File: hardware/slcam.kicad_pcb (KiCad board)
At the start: 4 copper layers, 42.2 x 25.4 mm, 33 parts, among them J1 532610671, J2 Conn_01x08, J3 Conn_01x04, J4 532610371, J5 532610371, U1 STM32F103C8Tx, U2 W25Q128JVS, U3 TCAN330G, U4 TPS2044D, Y1 Crystal_GND24

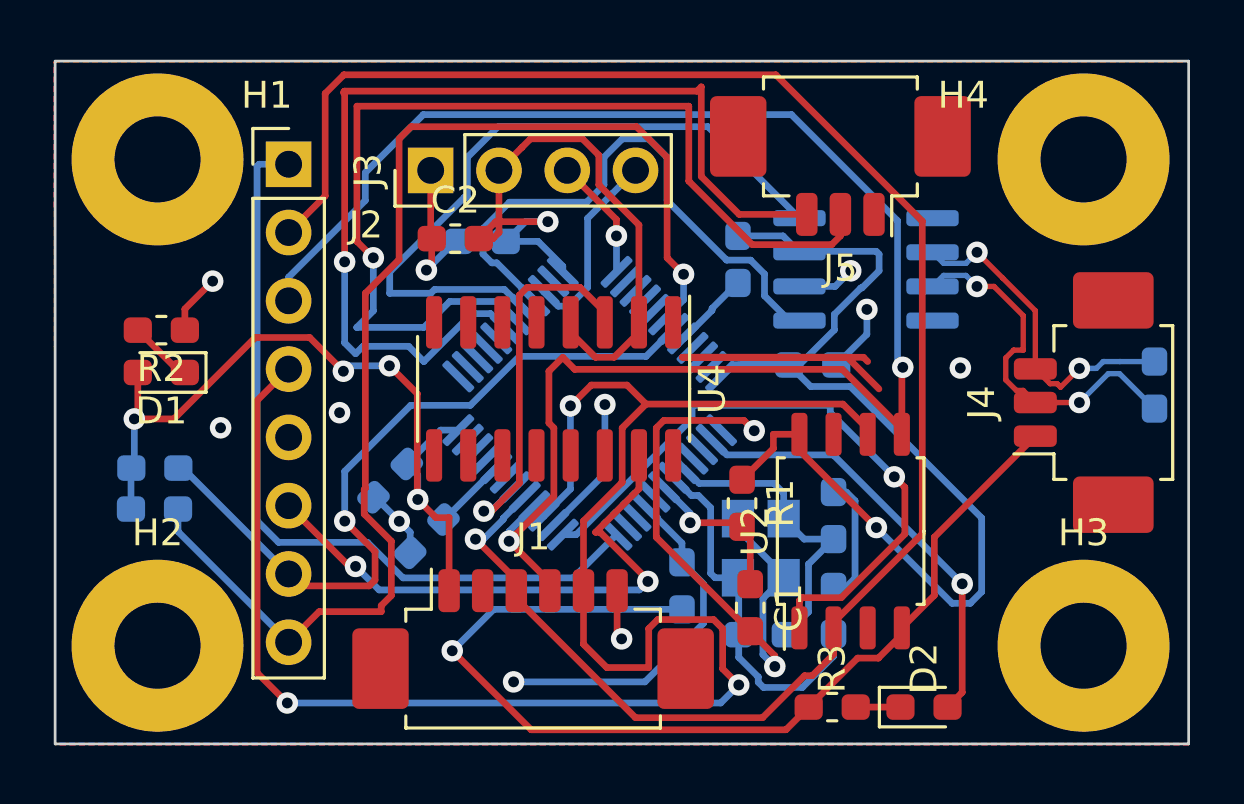
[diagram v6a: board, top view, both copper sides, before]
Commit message: hardware: Fixing the position of some labels in the layout #29
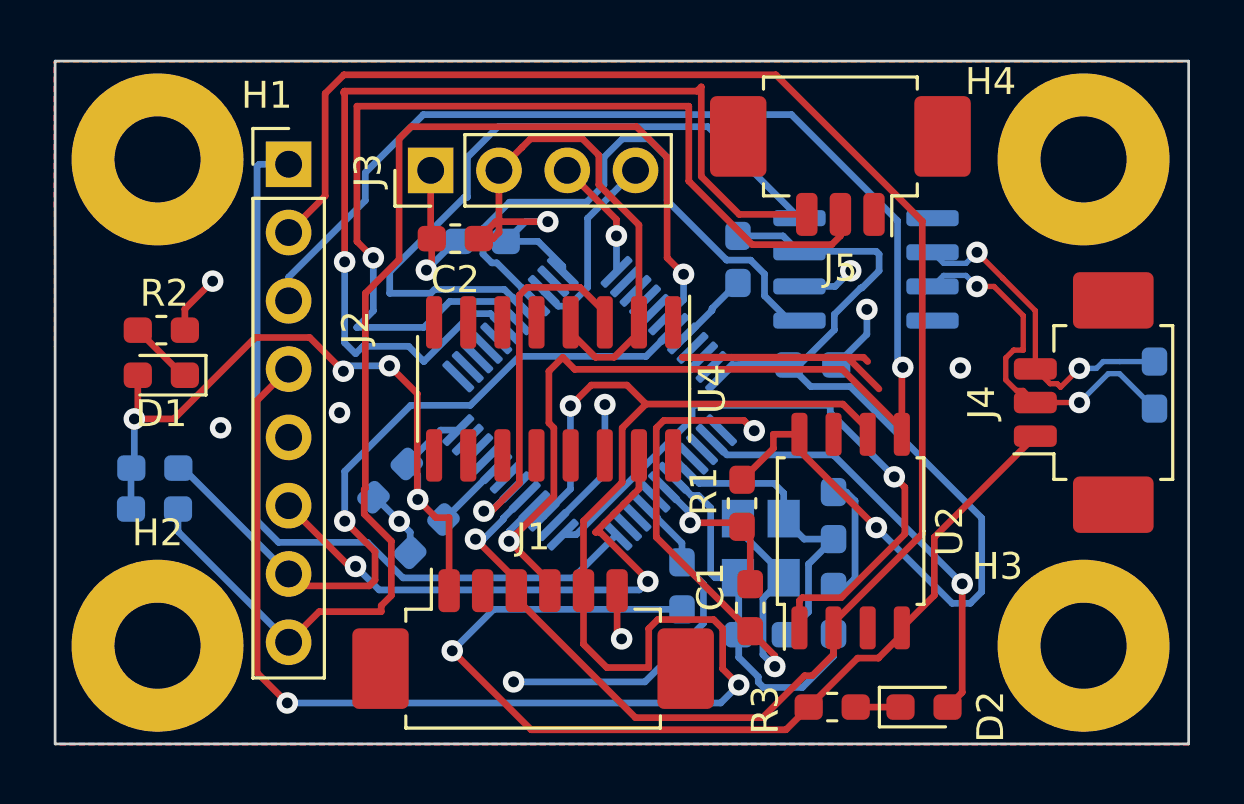
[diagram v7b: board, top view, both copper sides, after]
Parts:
- moved D1 0.10 mm to (201.1, 61.5)
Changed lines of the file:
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@@
     (tags "Through hole pin header THT 1x08 2.54mm single row")
     (attr through_hole)
-    (fp_text reference "J2" (at 2.871 2.26) (layer "F.SilkS")
+    (fp_text reference "J2" (at 2.49 6.07 90) (layer "F.SilkS")
       (effects (font (size 1 1) (thickness 0.15)))
     )
@@
     (tags "SOIC SO")
     (attr smd)
-    (fp_text reference "U2" (at 0 -3.56 270) (layer "F.SilkS")
+    (fp_text reference "U2" (at 0 3.683 270) (layer "F.SilkS")
       (effects (font (size 1 1) (thickness 0.15)))
     )
@@
     (tags "mounting hole 3.2mm m3")
     (attr exclude_from_pos_files exclude_from_bom)
-    (fp_text reference "H3" (at 0 -4.2) (layer "F.SilkS")
+    (fp_text reference "H3" (at -3.204 -2.95) (layer "F.SilkS")
       (effects (font (size 1 1) (thickness 0.15)))
     )
@@
     (tags "mounting hole 3.2mm m3")
     (attr exclude_from_pos_files exclude_from_bom)
-    (fp_text reference "H4" (at -4.474 -2.386) (layer "F.SilkS")
+    (fp_text reference "H4" (at -3.458 -2.894) (layer "F.SilkS")
       (effects (font (size 1 1) (thickness 0.15)))
     )
@@
     (tags "capacitor handsolder")
     (attr smd)
-    (fp_text reference "C1" (at 0 -1.43 90) (layer "F.SilkS")
+    (fp_text reference "C1" (at -0.7734 1.4732 90) (layer "F.SilkS")
       (effects (font (size 1 1) (thickness 0.15)))
     )
@@
   )
   (footprint "LED_SMD:LED_0603_1608Metric_Pad1.05x0.95mm_HandSolder" (layer "F.Cu")
-    (at 201.055 61.3664 180)
+    (at 201.055 61.468 180)
     (descr "LED SMD 0603 (1608 Metric), square (rectangular) end terminal, IPC_7351 nominal, (Body size source: http://www.tortai-tech.com/upload/download/2011102023233369053.pdf), generated with kicad-footprint-generator")
     (tags "LED handsolder")
@@
     (tags "resistor handsolder")
     (attr smd)
-    (fp_text reference "R1" (at 0 -1.43 90) (layer "F.SilkS")
+    (fp_text reference "R1" (at -0.4458 1.4224 90) (layer "F.SilkS")
       (effects (font (size 1 1) (thickness 0.15)))
     )
@@
     (tags "resistor handsolder")
     (attr smd)
-    (fp_text reference "R2" (at 0 -1.43) (layer "F.SilkS")
+    (fp_text reference "R2" (at -0.113 1.3716) (layer "F.SilkS")
       (effects (font (size 1 1) (thickness 0.15)))
     )
@@
     (tags "resistor handsolder")
     (attr smd)
-    (fp_text reference "R3" (at 0 -1.43 90) (layer "F.SilkS")
+    (fp_text reference "R3" (at -2.4892 0.1016 90) (layer "F.SilkS")
       (effects (font (size 1 1) (thickness 0.15)))
     )
@@
     (tags "capacitor handsolder")
     (attr smd)
-    (fp_text reference "C2" (at 0 -1.43) (layer "F.SilkS")
+    (fp_text reference "C2" (at 0 1.524) (layer "F.SilkS")
       (effects (font (size 1 1) (thickness 0.15)))
     )
@@
     (tags "LED handsolder")
     (attr smd)
-    (fp_text reference "D2" (at 0 -1.43 270) (layer "F.SilkS")
+    (fp_text reference "D2" (at 2.4778 0.3556 270) (layer "F.SilkS")
       (effects (font (size 1 1) (thickness 0.15)))
     )
@@
     (tags "LQFP QFP")
     (attr smd)
-    (fp_text reference "U1" (at 0 5.85 315) (layer "B.SilkS")
+    (fp_text reference "U1" (at 5.817759 -0.031582 45) (layer "B.SilkS")
       (effects (font (size 1 1) (thickness 0.15)) (justify mirror))
     )
@@
     (tags "SMD SMT crystal")
     (attr smd)
-    (fp_text reference "Y1" (at 0 2.45 90) (layer "B.SilkS")
+    (fp_text reference "Y1" (at -2.878 0.088 180) (layer "B.SilkS")
       (effects (font (size 1 1) (thickness 0.15)) (justify mirror))
     )
@@
     (tags "SOIC SO")
     (attr smd)
-    (fp_text reference "U3" (at 0 3.4) (layer "B.SilkS")
+    (fp_text reference "U3" (at 0 -3.429) (layer "B.SilkS")
       (effects (font (size 1 1) (thickness 0.15)) (justify mirror))
     )
@@
     (tags "resistor handsolder")
     (attr smd)
-    (fp_text reference "R4" (at 0 1.43 90) (layer "B.SilkS")
+    (fp_text reference "R4" (at -0.7734 1.43 90) (layer "B.SilkS")
       (effects (font (size 1 1) (thickness 0.15)) (justify mirror))
     )
@@
     (tags "resistor handsolder")
     (attr smd)
-    (fp_text reference "R7" (at 0 1.43) (layer "B.SilkS")
+    (fp_text reference "R7" (at 0.6096 -1.4224) (layer "B.SilkS")
       (effects (font (size 1 1) (thickness 0.15)) (justify mirror))
     )
@@
     (tags "resistor handsolder")
     (attr smd)
-    (fp_text reference "R8" (at 0 1.43 270) (layer "B.SilkS")
+    (fp_text reference "R8" (at 0.113 -1.524 270) (layer "B.SilkS")
       (effects (font (size 1 1) (thickness 0.15)) (justify mirror))
     )
@@
     (tags "capacitor handsolder")
     (attr smd)
-    (fp_text reference "C4" (at 0 1.43) (layer "B.SilkS")
+    (fp_text reference "C4" (at 2.681 0.1016) (layer "B.SilkS")
       (effects (font (size 1 1) (thickness 0.15)) (justify mirror))
     )
@@
   (segment (start 213.614 56.1624) (end 213.614 56.134) (width 0.25) (layer "F.Cu") (net 33))
   (segment (start 217.329001 54.386591) (end 217.329001 53.283999) (width 0.25) (layer "F.Cu") (net 33))
+  (segment (start 200.18 62.964) (end 200.0504 63.0936) (width 0.25) (layer "F.Cu") (net 33))
   (segment (start 218.821 59.501) (end 218.821 59.877072) (width 0.25) (layer "F.Cu") (net 33))
   (segment (start 213.614 53.848) (end 213.614 56.134) (width 0.25) (layer "F.Cu") (net 33))
@@
   (segment (start 218.821 59.877072) (end 217.897552 60.80052) (width 0.25) (layer "F.Cu") (net 33))
   (segment (start 223.8222 63.666) (end 223.8222 64.191) (width 0.25) (layer "F.Cu") (net 33))
-  (segment (start 200.18 61.3664) (end 200.18 62.964) (width 0.25) (layer "F.Cu") (net 33))
   (segment (start 211.266804 66.764613) (end 210.592701 66.09051) (width 0.25) (layer "F.Cu") (net 33))
   (segment (start 227.652581 67.134899) (end 224.79 64.272318) (width 0.25) (layer "F.Cu") (net 33))
+  (segment (start 200.18 61.468) (end 200.18 62.964) (width 0.25) (layer "F.Cu") (net 33))
   (segment (start 214.463999 52.998001) (end 213.614 53.848) (width 0.25) (layer "F.Cu") (net 33))
   (segment (start 209.539521 61.11767) (end 210.57648 62.154629) (width 0.25) (layer "F.Cu") (net 33))
-  (segment (start 200.18 62.964) (end 200.0504 63.0936) (width 0.25) (layer "F.Cu") (net 33))
   (segment (start 223.8222 64.191) (end 222.6564 65.3568) (width 0.25) (layer "F.Cu") (net 33))
   (segment (start 201.522616 63.0936) (end 200.0504 63.0936) (width 0.25) (layer "F.Cu") (net 33))
@@
   (segment (start 215.067484 56.4896) (end 215.989321 57.411437) (width 0.25) (layer "B.Cu") (net 33))
   (segment (start 200.0504 64.8094) (end 199.9374 64.9224) (width 0.25) (layer "B.Cu") (net 33))
-  (segment (start 201.93 61.3664) (end 201.7548 61.3664) (width 0.25) (layer "F.Cu") (net 34))
-  (segment (start 201.7548 61.3664) (end 200.18 59.7916) (width 0.25) (layer "F.Cu") (net 34))
+  (segment (start 201.93 61.468) (end 201.8564 61.468) (width 0.25) (layer "F.Cu") (net 34))
+  (segment (start 201.93 61.3664) (end 201.93 61.468) (width 0.25) (layer "F.Cu") (net 34))
+  (segment (start 201.8564 61.468) (end 200.18 59.7916) (width 0.25) (layer "F.Cu") (net 34))
   (segment (start 228.5492 73.8124) (end 226.8842 73.8124) (width 0.25) (layer "F.Cu") (net 35))
   (segment (start 218.009 69.482) (end 218.009 71.107872) (width 0.25) (layer "F.Cu") (net 36))

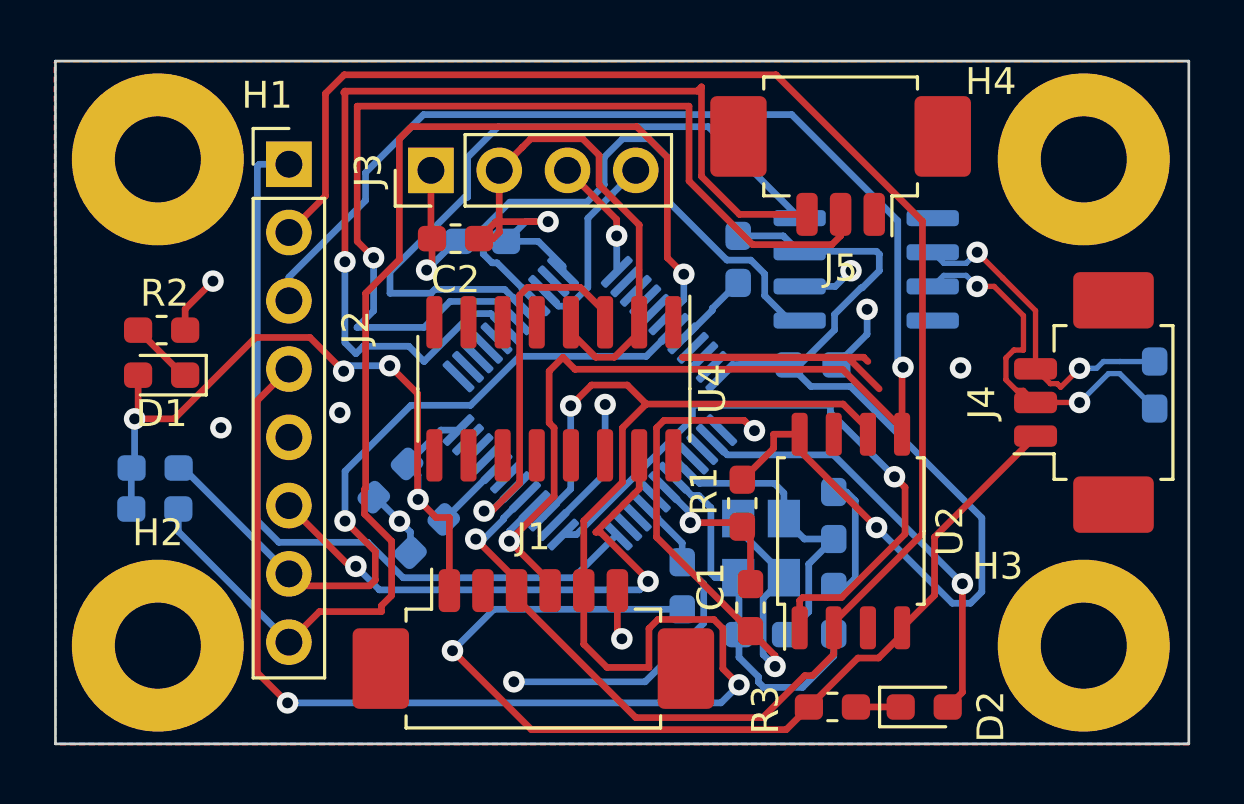
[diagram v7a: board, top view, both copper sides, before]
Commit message: hardware: Improving PCB tracks #29
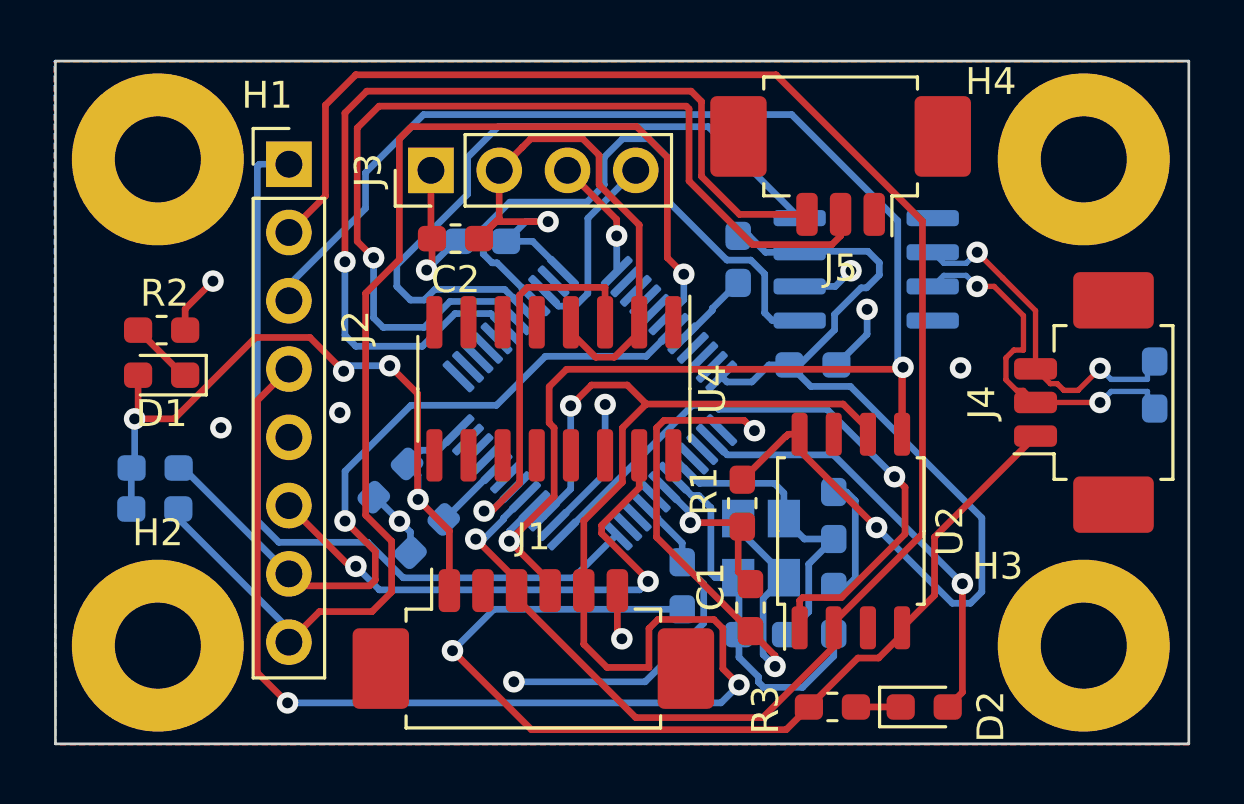
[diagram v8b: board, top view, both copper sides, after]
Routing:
- net (no net): track 14.8 -> 0.00 mm
- net /UART_TX: track 38.1 -> 36.3 mm
- net /UART_RX: track 38.0 -> 36.4 mm
- net GND: track 146.4 -> 145.4 mm
- net /CAN_N: track 12.3 -> 13.3 mm
- net VCC: track 109.3 -> 108.4 mm
- net /SPI_MISO: track 62.2 -> 62.8 mm
- net /EN_SWITCH: track 14.3 -> 14.9 mm
